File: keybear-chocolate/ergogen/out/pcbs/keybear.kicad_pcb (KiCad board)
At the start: 2 copper layers, 136.9 x 97.5 mm, 46 parts

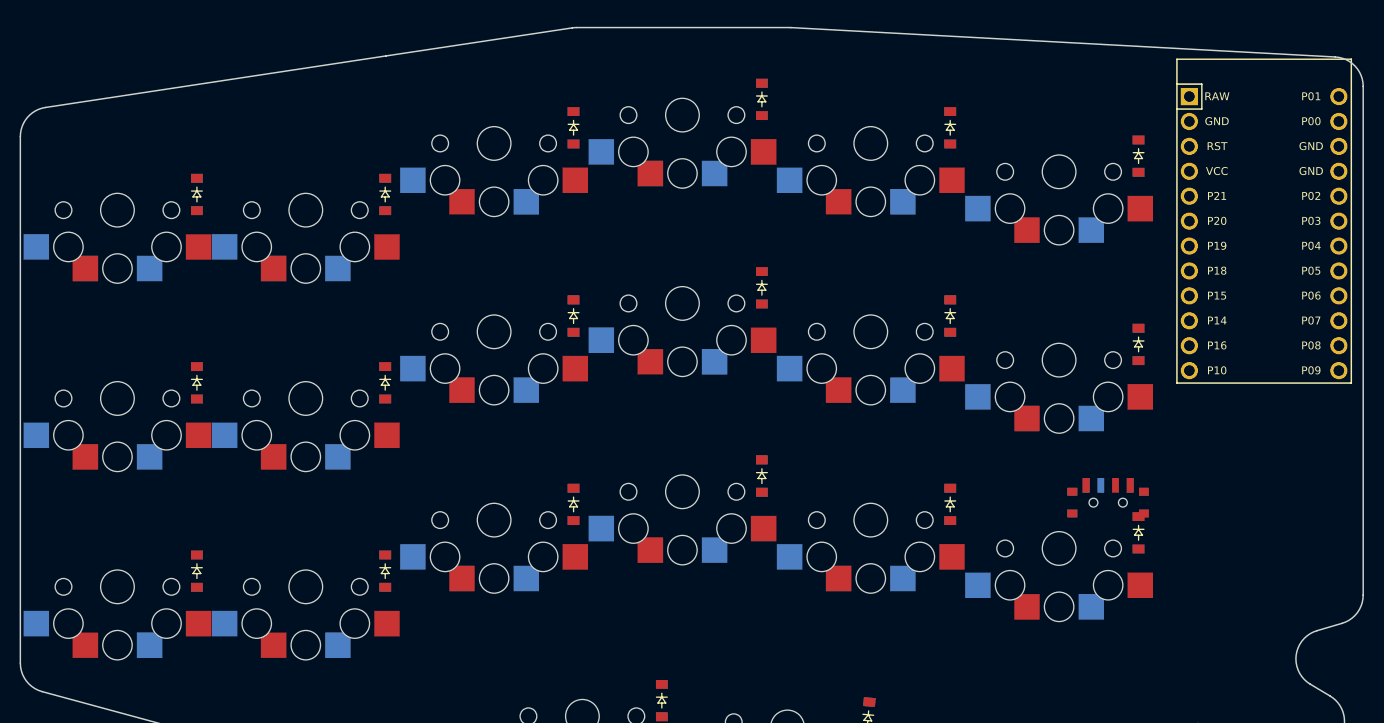
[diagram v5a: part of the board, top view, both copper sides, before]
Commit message: small changes to the outline onthe upper side of the pcb
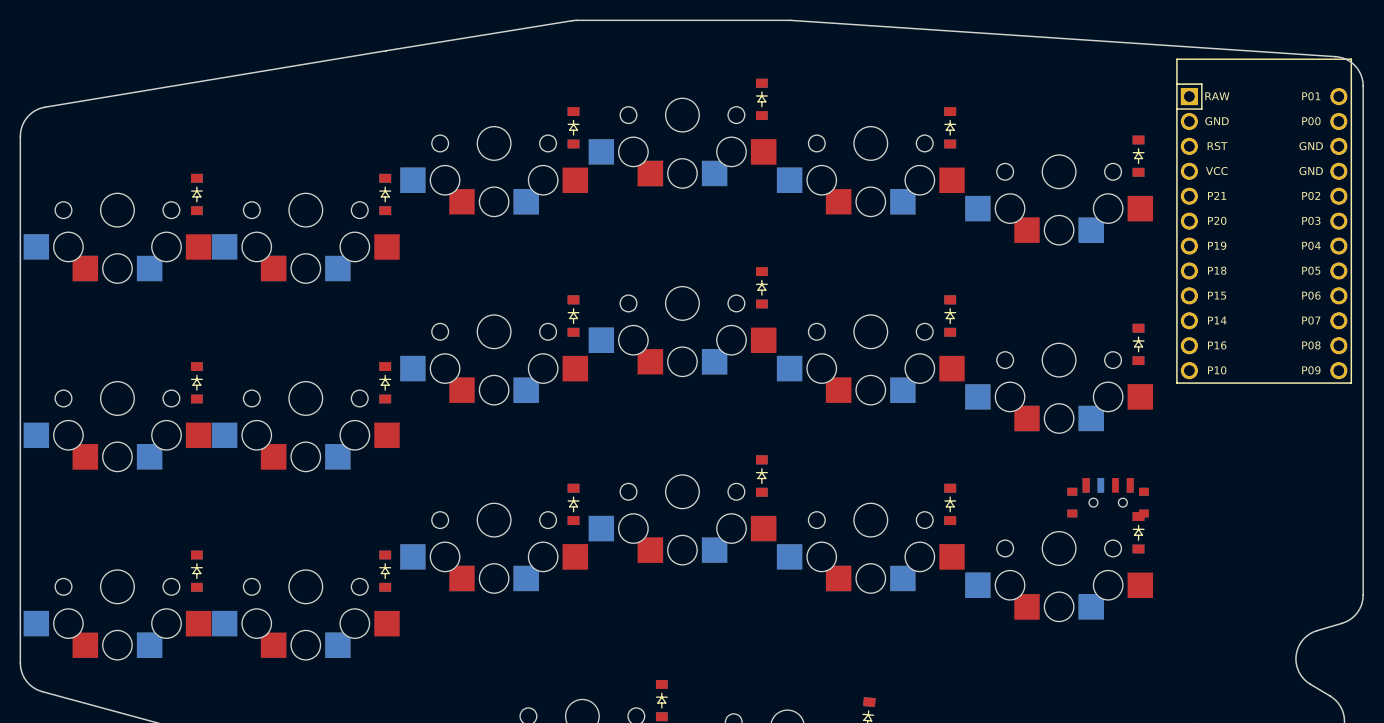
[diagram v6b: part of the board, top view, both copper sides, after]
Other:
- board size 136.9 x 97.5 mm -> 136.9 x 98.2 mm
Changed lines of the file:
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@@
       (pad "" smd rect (at 3.65 -0.78) (size 1 0.8) (layers B.Cu B.Paste B.Mask))
         )
-            (gr_line (start 140.1 157.78587581336933) (end 140.1 104.10013996290886) (angle 90) (layer Edge.Cuts) (width 0.15))
-(gr_line (start 142.65109021703427 101.13391677546493) (end 177.3988203601405 95.87517852726559) (angle 90) (layer Edge.Cuts) (width 0.15))
-(gr_line (start 177.4011978556094 95.87481969777545) (end 196.37798433395645 93.01841798306593) (angle 90) (layer Edge.Cuts) (width 0.15))
-(gr_line (start 196.82451662145328 92.985) (end 218.5190226483359 92.985) (angle 90) (layer Edge.Cuts) (width 0.15))
-(gr_line (start 218.68085854833595 92.9893683) (end 274.1618359 95.98667110041953) (angle 90) (layer Edge.Cuts) (width 0.15))
-(gr_line (start 277 150.84469349561692) (end 277 98.98230280041953) (angle 90) (layer Edge.Cuts) (width 0.15))
+            (gr_line (start 140.1 157.78587581336933) (end 140.1 104.06451984563004) (angle 90) (layer Edge.Cuts) (width 0.15))
+(gr_line (start 142.61040631876435 101.10473975906767) (end 177.3943013369031 95.35094264748813) (angle 90) (layer Edge.Cuts) (width 0.15))
+(gr_line (start 177.40571270240318 95.34907763659115) (end 196.36244705523208 92.28835490254066) (angle 90) (layer Edge.Cuts) (width 0.15))
+(gr_line (start 196.8406293709677 92.25) (end 218.50019635963994 92.25) (angle 90) (layer Edge.Cuts) (width 0.15))
+(gr_line (start 218.6995832662715 92.25663320044171) (end 274.19938690663156 95.95345231278762) (angle 90) (layer Edge.Cuts) (width 0.15))
+(gr_line (start 277 150.84469349561692) (end 277 98.94681911234589) (angle 90) (layer Edge.Cuts) (width 0.15))
 (gr_line (start 274.8457699349969 153.7230043147176) (end 272.29609492614367 154.47220715426178) (angle 90) (layer Edge.Cuts) (width 0.15))
 (gr_line (start 271.60438377888295 159.92659094363484) (end 273.63274875310157 161.1371828691278) (angle 90) (layer Edge.Cuts) (width 0.15))
@@
 (gr_line (start 208.6068056042486 172.92901137144023) (end 186.7808016494666 172.65478447879255) (angle 90) (layer Edge.Cuts) (width 0.15))
 (gr_line (start 186.03247292294077 172.5502199706558) (end 142.31398167471463 160.68107450650461) (angle 90) (layer Edge.Cuts) (width 0.15))
-(gr_arc (start 143.1 104.10013996290886) (end 142.6510902 101.13391676290885) (angle -81.39413273346547) (layer Edge.Cuts) (width 0.15))
-(gr_arc (start 177.84773014310622 98.84140171470952) (end 177.40119784310622 95.87481971470952) (angle -0.045921071564606564) (layer Edge.Cuts) (width 0.15))
-(gr_arc (start 196.82451662145328 95.985) (end 196.82451662145328 92.985) (angle -8.559946194970465) (layer Edge.Cuts) (width 0.15))
-(gr_arc (start 218.5190226483359 95.985) (end 218.6808585483359 92.9893683) (angle -3.0923390625223277) (layer Edge.Cuts) (width 0.15))
-(gr_arc (start 274 98.98230280041953) (end 277 98.98230280041953) (angle -86.90766093747821) (layer Edge.Cuts) (width 0.15))
+(gr_arc (start 143.1 104.06451984563004) (end 142.6104063 101.10473974563004) (angle -80.60743764638079) (layer Edge.Cuts) (width 0.15))
+(gr_arc (start 177.88389501813876 98.31072273405049) (end 177.40571271813877 95.34907763405049) (angle -0.22083267533345463) (layer Edge.Cuts) (width 0.15))
+(gr_arc (start 196.8406293709677 95.25) (end 196.8406293709677 92.25) (angle -9.171729678286312) (layer Edge.Cuts) (width 0.15))
+(gr_arc (start 218.50019635963994 95.25) (end 218.69958325963995 92.2566332) (angle -3.8108184948550416) (layer Edge.Cuts) (width 0.15))
+(gr_arc (start 274 98.94681911234589) (end 277 98.94681911234589) (angle -86.18918150514494) (layer Edge.Cuts) (width 0.15))
 (gr_arc (start 274 150.84469349561692) (end 274.8457699 153.72300429561693) (angle -73.62497240499397) (layer Edge.Cuts) (width 0.15))
 (gr_arc (start 273.14186486114056 157.35051797336246) (end 272.29609496114057 154.47220717336245) (angle -132.7948957837653) (layer Edge.Cuts) (width 0.15))
